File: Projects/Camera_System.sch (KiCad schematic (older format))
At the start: 10 parts, among them J1 BARREL_JACK, U1 IFX1117ME_V33, U2 LD2980ABM50TR

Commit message: Component and footprint library created
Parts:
- U1: footprint (none) -> MyLibraries:IFX1117ME_V33
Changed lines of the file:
@@
 LIBS:atmel
 LIBS:contrib
+LIBS:valves
 LIBS:MyLibrary
-LIBS:valves
 LIBS:Camera_System-cache
 EELAYER 25 0
@@
 Text Notes 3250 1200 0    60   ~ 0
 6 < VIN < 15
-$Comp
-L IFX1117ME_V33 U1
-U 1 1 59131708
-P 4450 1150
-F 0 "U1" H 4450 1250 60  0000 C CNN
-F 1 "IFX1117ME_V33" H 4450 1400 60  0000 C CNN
-F 2 "" H 4450 1150 60  0001 C CNN
-F 3 "" H 4450 1150 60  0001 C CNN
-	1    4450 1150
-	1    0    0    -1
-$EndComp
 Wire Wire Line
 	5000 1300 5900 1300
@@
 Wire Wire Line
 	5900 2850 5900 2750
-$Comp
-L LD2980ABM50TR U2
-U 1 1 59132F80
-P 4450 2750
-F 0 "U2" H 4450 2900 60  0000 C CNN
-F 1 "LD2980ABM50TR" H 4450 3050 60  0000 C CNN
-F 2 "" H 4450 2750 60  0001 C CNN
-F 3 "" H 4450 2750 60  0001 C CNN
-	1    4450 2750
-	1    0    0    -1
-$EndComp
 Text Notes 4100 2350 0    60   ~ 0
 Order the one with fixed output voltage = 5V
@@
 Text Label 2600 1300 0    60   ~ 0
 VDC_IN
+$Comp
+L IFX1117ME_V33 U1
+U 1 1 59135F80
+P 4450 1150
+F 0 "U1" H 4450 1250 60  0000 C CNN
+F 1 "IFX1117ME_V33" H 4450 1400 60  0000 C CNN
+F 2 "MyLibraries:IFX1117ME_V33" H 4450 1150 60  0001 C CNN
+F 3 "" H 4450 1150 60  0001 C CNN
+	1    4450 1150
+	1    0    0    -1
+$EndComp
+$Comp
+L LD2980ABM50TR U2
+U 1 1 59135FEA
+P 4450 2750
+F 0 "U2" H 4450 2900 60  0000 C CNN
+F 1 "LD2980ABM50TR" H 4450 3050 60  0000 C CNN
+F 2 "" H 4450 2750 60  0001 C CNN
+F 3 "" H 4450 2750 60  0001 C CNN
+	1    4450 2750
+	1    0    0    -1
+$EndComp
 $EndSCHEMATC

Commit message: Power Management Layout Created
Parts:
- removed D1: CS3D, symbol D
- added D1: CS3M, MyLibraries:CS3M, symbol CS3M
- C1: footprint (none) -> MyLibraries:UWT1E470MCL6GS
- C2: footprint (none) -> MyLibraries:UWX1E100MCL1GB
- C3, C4, C6: footprint (none) -> Capacitors_SMD:C_0603_HandSoldering
- C5: footprint (none) -> Capacitors_SMD:C_0805_HandSoldering
- J1: footprint (none) -> MyLibraries:PJ-002B
- U2: footprint (none) -> MyLibraries:LD2980ABM50TR
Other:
- note added: "I_out = 1.1A"
- note added: "I_out = 50mA"
- note removed: "I_out_min = 1.1A"
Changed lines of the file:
@@
 F 0 "J1" H 1050 1595 50  0000 C CNN
 F 1 "BARREL_JACK" H 1050 1245 50  0000 C CNN
-F 2 "" H 1050 1400 50  0001 C CNN
+F 2 "MyLibraries:PJ-002B" H 1050 1400 50  0001 C CNN
 F 3 "" H 1050 1400 50  0001 C CNN
 	1    1050 1400
@@
 Wire Wire Line
 	1350 1300 1900 1300
-$Comp
-L CP C1
-U 1 1 5912CF48
-P 2400 1650
-F 0 "C1" H 2425 1750 50  0000 L CNN
-F 1 "47u" H 2425 1550 50  0000 L CNN
-F 2 "" H 2438 1500 50  0001 C CNN
-F 3 "" H 2400 1650 50  0001 C CNN
-	1    2400 1650
-	1    0    0    -1
-$EndComp
 Wire Wire Line
 	2400 1300 2400 1500
@@
 Wire Wire Line
 	2400 1800 2400 1900
-$Comp
-L D D1
-U 1 1 5912D262
-P 2050 1300
-F 0 "D1" H 2050 1400 50  0000 C CNN
-F 1 "CS3D" H 2050 1200 50  0000 C CNN
-F 2 "" H 2050 1300 50  0001 C CNN
-F 3 "" H 2050 1300 50  0001 C CNN
-	1    2050 1300
-	-1   0    0    1
-$EndComp
 Connection ~ 2400 1300
 Wire Wire Line
 	2200 1300 3900 1300
-Wire Wire Line
-	5550 1500 5550 1300
 Wire Wire Line
 	5550 1800 5550 1900
@@
 F 0 "C4" H 3625 1750 50  0000 L CNN
 F 1 "100n" H 3625 1550 50  0000 L CNN
-F 2 "" H 3638 1500 50  0001 C CNN
+F 2 "Capacitors_SMD:C_0603_HandSoldering" H 3638 1500 50  0001 C CNN
 F 3 "" H 3600 1650 50  0001 C CNN
 	1    3600 1650
@@
 Order the one with fixed output voltage = 3.3V
 Text Notes 5000 1200 0    60   ~ 0
-I_out_min = 1.1A
+I_out = 1.1A
 $Comp
 L CP C2
@@
 F 0 "C2" H 3275 1750 50  0000 L CNN
 F 1 "10u" H 3275 1550 50  0000 L CNN
-F 2 "" H 3288 1500 50  0001 C CNN
+F 2 "MyLibraries:UWX1E100MCL1GB" H 3288 1500 50  0001 C CNN
 F 3 "" H 3250 1650 50  0001 C CNN
 	1    3250 1650
@@
 F 0 "C6" H 5575 3300 50  0000 L CNN
 F 1 "2.2u" H 5575 3100 50  0000 L CNN
-F 2 "" H 5588 3050 50  0001 C CNN
+F 2 "Capacitors_SMD:C_0603_HandSoldering" H 5588 3050 50  0001 C CNN
 F 3 "" H 5550 3200 50  0001 C CNN
 	1    5550 3200
@@
 F 0 "C3" H 3275 3300 50  0000 L CNN
 F 1 "1u" H 3275 3100 50  0000 L CNN
-F 2 "" H 3288 3050 50  0001 C CNN
+F 2 "Capacitors_SMD:C_0603_HandSoldering" H 3288 3050 50  0001 C CNN
 F 3 "" H 3250 3200 50  0001 C CNN
 	1    3250 3200
@@
 F 0 "C5" H 5575 1750 50  0000 L CNN
 F 1 "22u" H 5575 1550 50  0000 L CNN
-F 2 "" H 5588 1500 50  0001 C CNN
+F 2 "Capacitors_SMD:C_0805_HandSoldering" H 5588 1500 50  0001 C CNN
 F 3 "" H 5550 1650 50  0001 C CNN
 	1    5550 1650
@@
 F 0 "U2" H 4450 2900 60  0000 C CNN
 F 1 "LD2980ABM50TR" H 4450 3050 60  0000 C CNN
-F 2 "" H 4450 2750 60  0001 C CNN
+F 2 "MyLibraries:LD2980ABM50TR" H 4450 2750 60  0001 C CNN
 F 3 "" H 4450 2750 60  0001 C CNN
 	1    4450 2750
 	1    0    0    -1
 $EndComp
+Text Notes 4950 2700 0    60   ~ 0
+I_out = 50mA
+$Comp
+L CS3M D1
+U 1 1 591418FD
+P 2050 1300
+F 0 "D1" H 2050 1400 50  0000 C CNN
+F 1 "CS3M" H 2050 1200 50  0000 C CNN
+F 2 "MyLibraries:CS3M" H 2050 1300 50  0001 C CNN
+F 3 "" H 2050 1300 50  0001 C CNN
+	1    2050 1300
+	-1   0    0    1
+$EndComp
+$Comp
+L CP C1
+U 1 1 591435A8
+P 2400 1650
+F 0 "C1" H 2425 1750 50  0000 L CNN
+F 1 "47u" H 2425 1550 50  0000 L CNN
+F 2 "MyLibraries:UWT1E470MCL6GS" H 2438 1500 50  0001 C CNN
+F 3 "" H 2400 1650 50  0001 C CNN
+	1    2400 1650
+	1    0    0    -1
+$EndComp
+Wire Wire Line
+	5550 1300 5550 1500
+Connection ~ 5550 1300
 $EndSCHEMATC

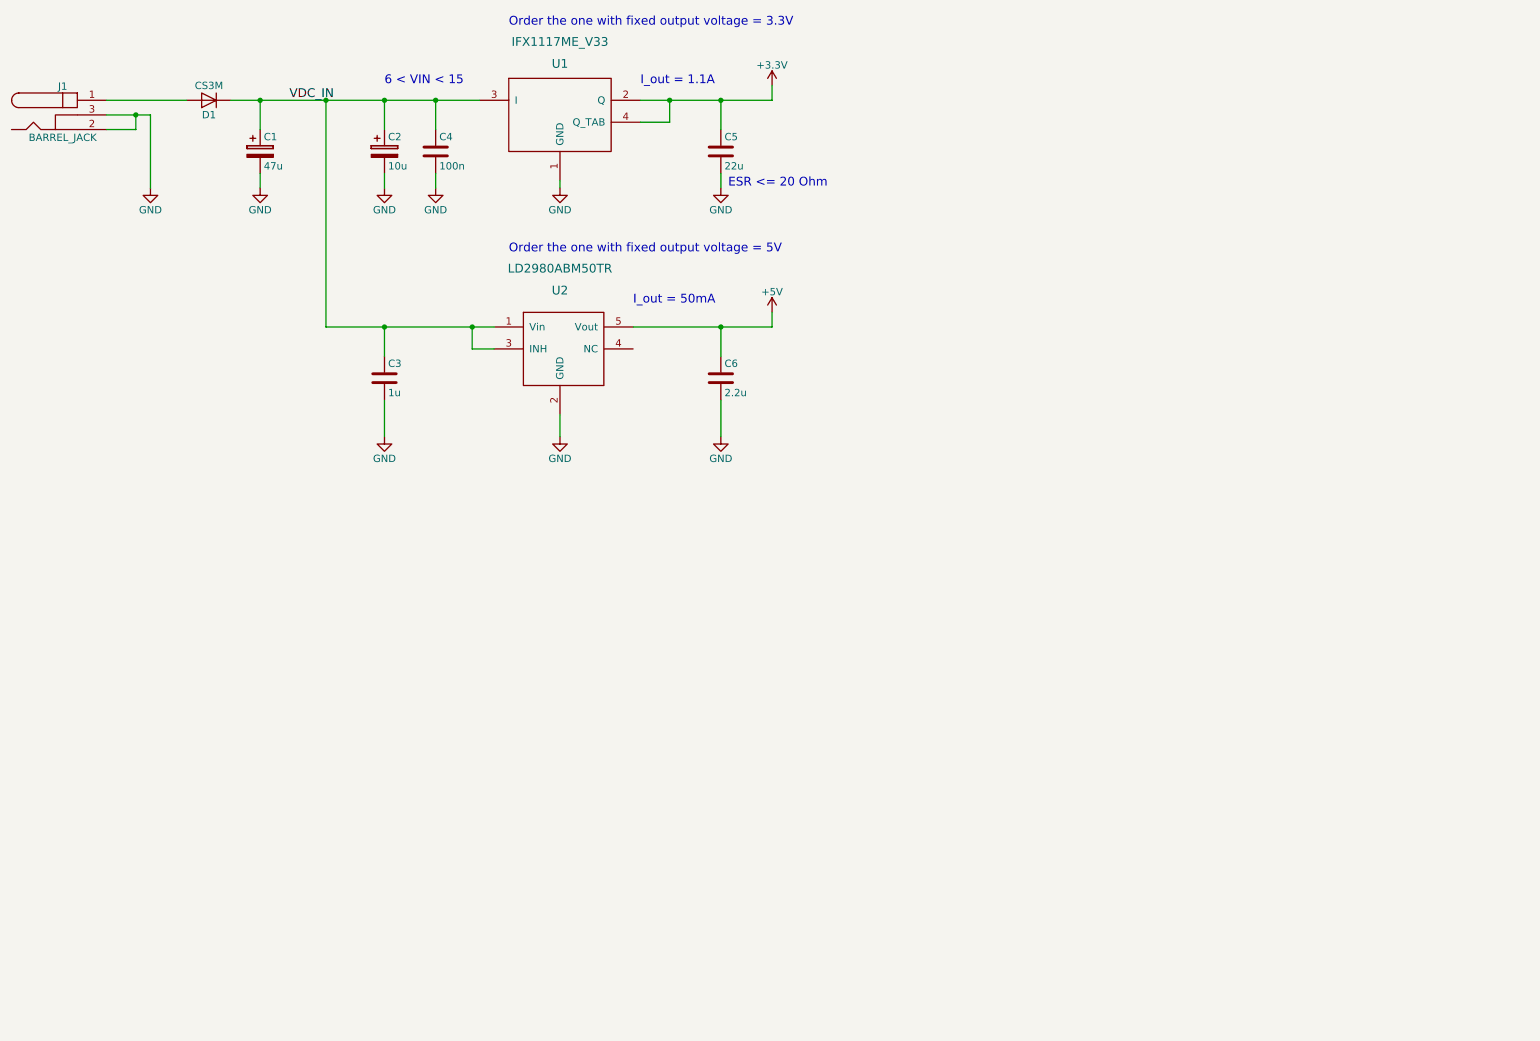
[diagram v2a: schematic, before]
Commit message: New symbols habe been added
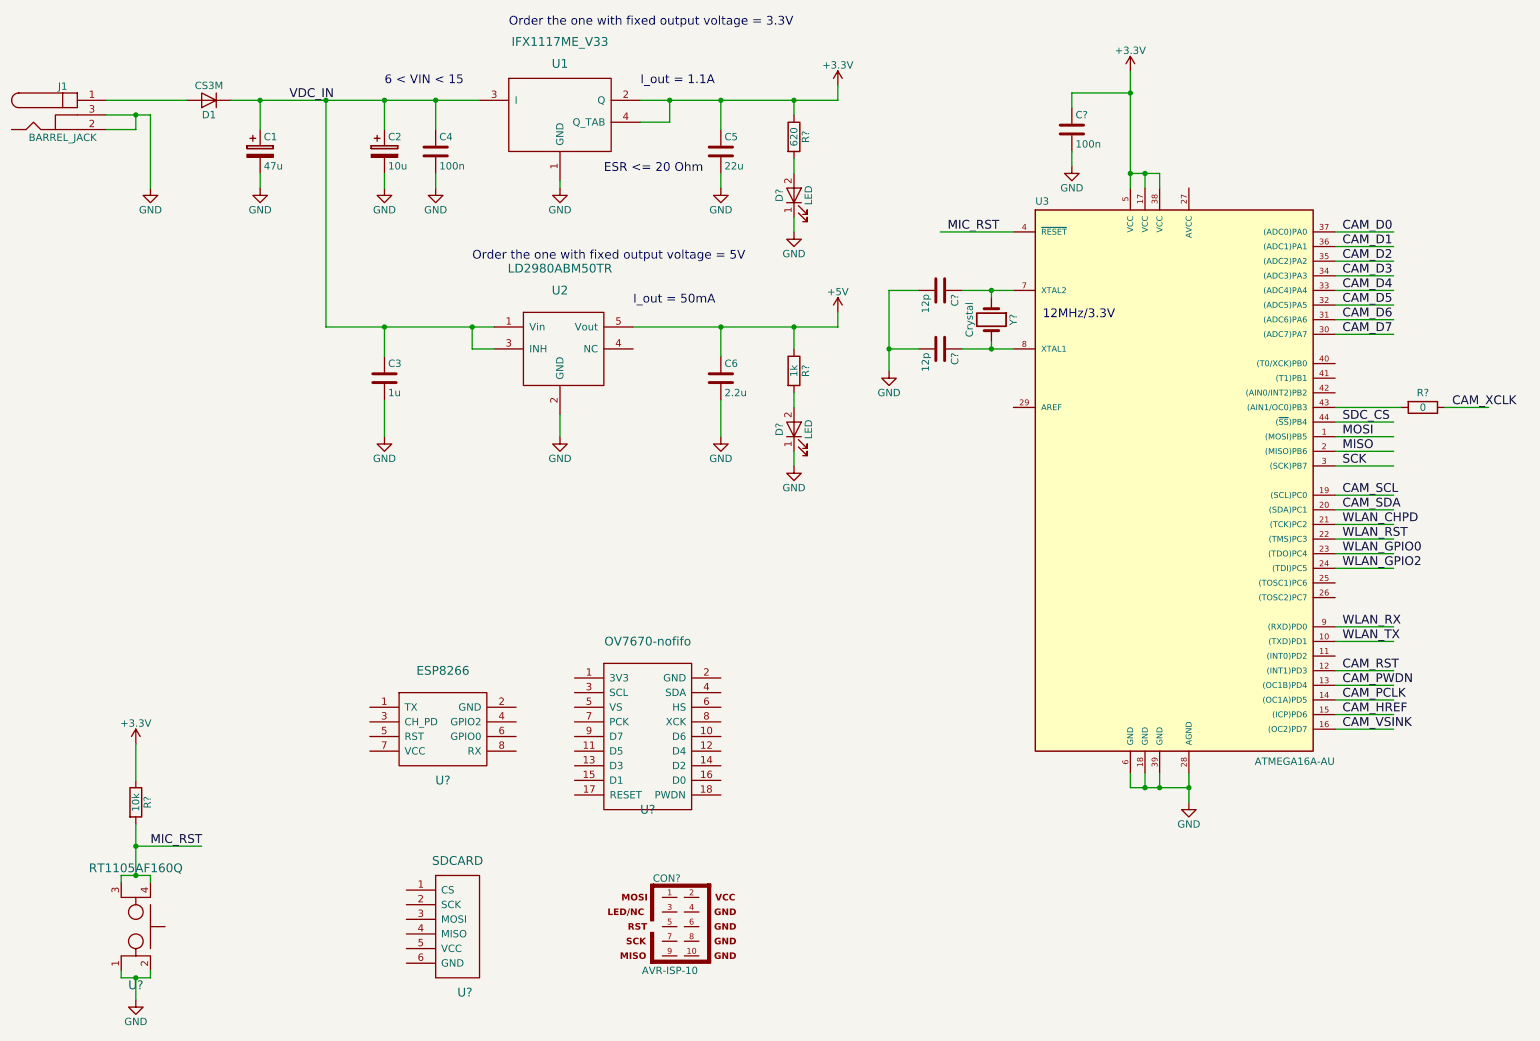
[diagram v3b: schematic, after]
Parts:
- added C?: 100n, Capacitors_SMD:C_0805_HandSoldering, symbol C
- added C? (x2): 12p, Capacitors_SMD:C_0603_HandSoldering, symbol C
- added CON?: AVR-ISP-10, AVR-ISP-10, symbol AVR-ISP-10
- added D? (x2): LED, symbol LED
- added R?: 620, symbol R
- added R?: 1k, symbol R
- added R?: 0, symbol R
- added R?: 10k, symbol R
- added U3: ATMEGA16A-AU, MyLibraries:ATMEGA16A-AU, symbol ATMEGA16A-AU
- added U?: RT1105AF160Q, symbol RT1105AF160Q
- added U?: ESP8266, symbol ESP8266
- added U?: OV7670-nofifo, symbol OV7670-nofifo
- added U?: SDCARD, symbol SDCARD
- added Y?: Crystal, symbol Crystal
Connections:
- net labels added: CAM_D0, CAM_D1, CAM_D2, CAM_D3, CAM_D4, CAM_D5, CAM_D6, CAM_D7, CAM_HREF, CAM_PCLK, CAM_PWDN, CAM_RST, CAM_SCL, CAM_SDA, CAM_VSINK, CAM_XCLK, MIC_RST, MISO, MOSI, SCK, SDC_CS, WLAN_CHPD, WLAN_GPIO0, WLAN_GPIO2, WLAN_RST, WLAN_RX, WLAN_TX
- wire segments 30 -> 93
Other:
- note added: "12MHz/3.3V\n"

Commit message: Schematic for additional modules have been created
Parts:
- removed U3: ATMEGA16A-AU, MyLibraries:ATMEGA16A-AU, symbol ATMEGA16A-AU
- added C? (x9): 100n, Capacitors_SMD:C_0805_HandSoldering, symbol C
- added D?: LED, symbol LED
- added R?: 620, symbol R
- added R? (x2): 4.7k, symbol R
- added R?: 24.9, symbol R
- added R? (x7): 10k, symbol R
- added R? (x2): 1.74k, symbol R
- added R?: 200k, symbol R
- added U?: ATMEGA16A-AU, TQFP44, symbol ATMEGA16A-AU
- added U?: Si501, symbol Si501
- added U?: CD4014B, symbol CD4014B
- added U? (x6): RT1105AF160Q, symbol RT1105AF160Q
- added U?: LCD_1602, symbol LCD_1602
- added U?: PCA9306, symbol PCA9306
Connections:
- net labels added: 3V3_SCL, 3V3_SDA, 5V_SCL, 5V_SDA, CAM_VSINC, CTRL_BTN1, CTRL_BTN2, CTRL_DOWN, CTRL_LEFT, CTRL_RIGHT, CTRL_UP, P_S_CLK, P_S_CTRL, SERIAL_IN
- net labels removed: CAM_SCL, CAM_SDA, CAM_VSINK
- wire segments 93 -> 271
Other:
- note added: "BUTTONS"
- note added: "CAMERA"
- note added: "LCD"
- note added: "Modules"
- note added: "SD CARD"
- note added: "WLAN"
- moved on the sheet: C?, CON?, R?, U?, Y?

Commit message: New footprints have been created
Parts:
- CON1: renamed from CON?; footprint AVR-ISP-10 -> MyLibraries:N2510-6002RB
- D2, D3, D4: renamed from D?; footprint (none) -> LEDs:LED_0603
- R1, R10, R11, R12, R13, R14, R15, R16, R17, R18, R2, R3, R4, R5, R6, R7, R8, R9: renamed from R?; footprint (none) -> Resistors_SMD:R_0603_HandSoldering
- U10, U11, U13, U4, U5, U6, U7: renamed from U?; footprint (none) -> MyLibraries:RT1105AF160Q
- U8: renamed from U?; footprint (none) -> MyLibraries:CD4014B_SOIC
- U9: renamed from U?; footprint (none) -> MyLibraries:PCA9306_SM8
- gave numbers to parts that had none: 19

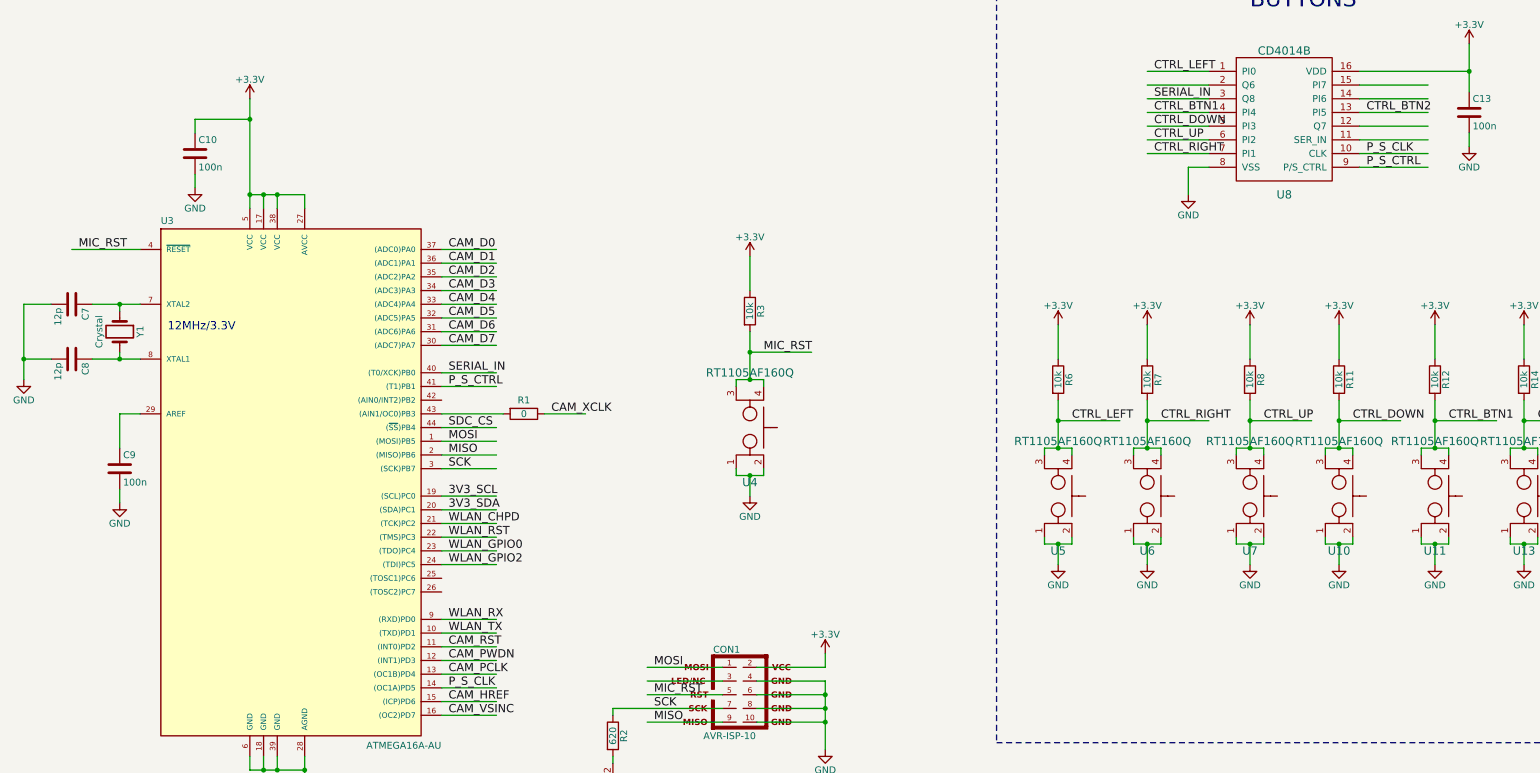
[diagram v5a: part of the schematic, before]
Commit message: Schematic has been finished and layout started
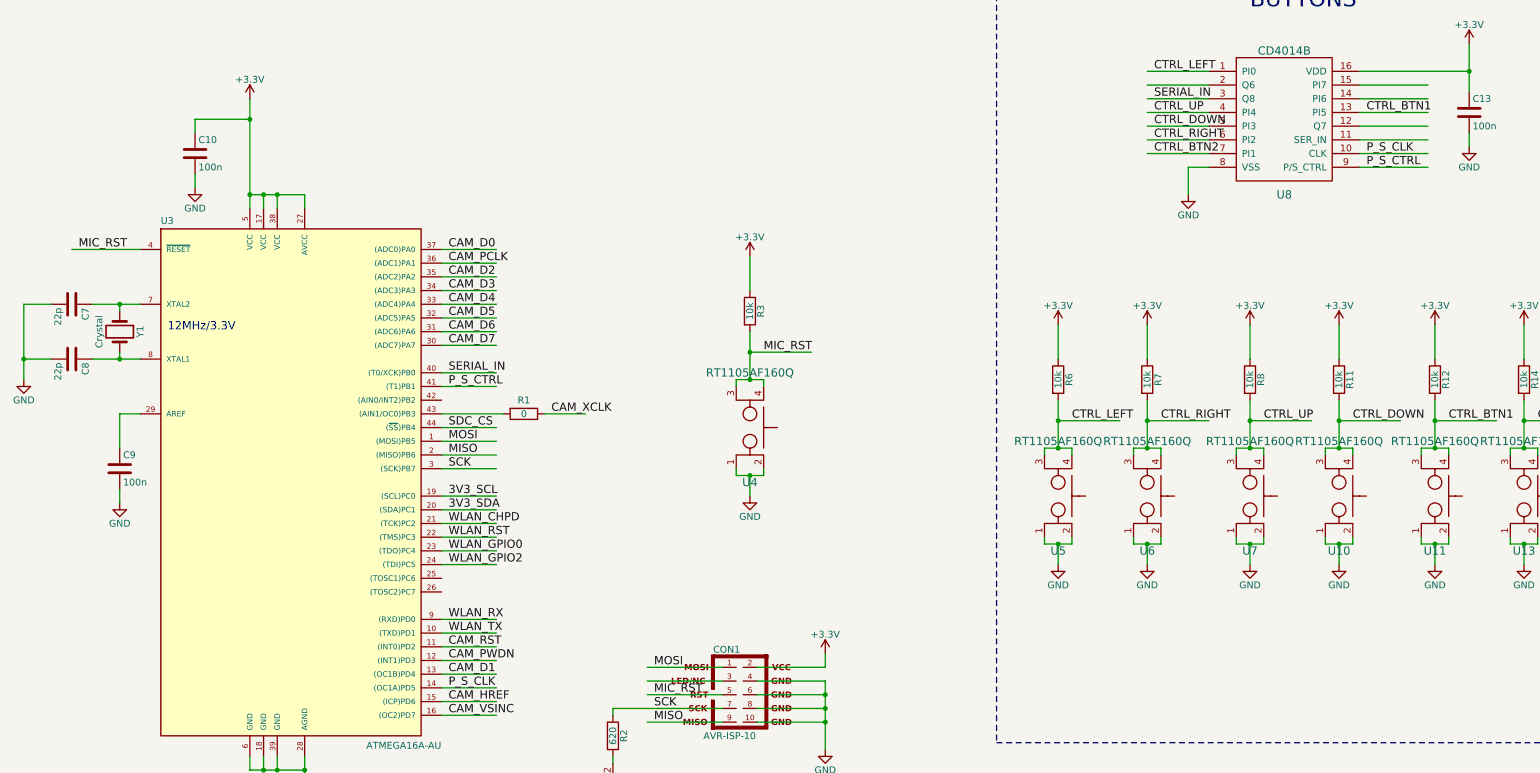
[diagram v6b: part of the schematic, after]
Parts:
- C7, C8: value 12p -> 22p
- U12: footprint (none) -> MyLibraries:LCD_header_2.5_4
- U14: footprint (none) -> MyLibraries:Si501_2x2.5
- U15: footprint (none) -> MyLibraries:Camera_ov7670_2.5_2x9
- U16: footprint (none) -> MyLibraries:wifi_header_female_2.5_2x4
- U17: footprint (none) -> MyLibraries:SDCARD_2.5_6
- U3: footprint TQFP44 -> MyLibraries:ATMEGA16A-AU
- Y1: footprint (none) -> MyLibraries:LFXTAL003210
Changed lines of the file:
@@
 Text Label 3800 6350 0    60   ~ 0
 CAM_D0
-Text Label 3800 6450 0    60   ~ 0
+Text Label 3800 9450 0    60   ~ 0
 CAM_D1
 Text Label 3800 6550 0    60   ~ 0
@@
 F 0 "Y1" H 1400 7100 50  0000 C CNN
 F 1 "Crystal" H 1400 6800 50  0000 C CNN
-F 2 "" H 1400 6950 50  0001 C CNN
+F 2 "MyLibraries:LFXTAL003210" H 1400 6950 50  0001 C CNN
 F 3 "" H 1400 6950 50  0001 C CNN
 	1    1400 6950
@@
 P 1050 6750
 F 0 "C7" H 1075 6850 50  0000 L CNN
-F 1 "12p" H 1075 6650 50  0000 L CNN
+F 1 "22p" H 1075 6650 50  0000 L CNN
 F 2 "Capacitors_SMD:C_0603_HandSoldering" H 1088 6600 50  0001 C CNN
 F 3 "" H 1050 6750 50  0001 C CNN
@@
 P 1050 7150
 F 0 "C8" H 1075 7250 50  0000 L CNN
-F 1 "12p" H 1075 7050 50  0000 L CNN
+F 1 "22p" H 1075 7050 50  0000 L CNN
 F 2 "Capacitors_SMD:C_0603_HandSoldering" H 1088 7000 50  0001 C CNN
 F 3 "" H 1050 7150 50  0001 C CNN
@@
 Text Label 3800 9350 0    60   ~ 0
 CAM_PWDN
-Text Label 3800 9450 0    60   ~ 0
+Text Label 3800 6450 0    60   ~ 0
 CAM_PCLK
 Text Label 3800 9650 0    60   ~ 0
@@
 F 0 "U16" H 14300 5300 60  0000 C CNN
 F 1 "ESP8266" H 14300 6050 60  0000 C CNN
-F 2 "" H 14300 5900 60  0001 C CNN
+F 2 "MyLibraries:wifi_header_female_2.5_2x4" H 14300 5900 60  0001 C CNN
 F 3 "" H 14300 5900 60  0001 C CNN
 	1    14300 5900
@@
 F 0 "U15" H 14200 1000 60  0000 C CNN
 F 1 "OV7670-nofifo" H 14200 2250 60  0000 C CNN
-F 2 "" H 14200 2100 60  0001 C CNN
+F 2 "MyLibraries:Camera_ov7670_2.5_2x9" H 14200 2100 60  0001 C CNN
 F 3 "" H 14200 2100 60  0001 C CNN
 	1    14200 2100
@@
 F 0 "U17" H 14600 7400 60  0000 C CNN
 F 1 "SDCARD" H 14550 8300 60  0000 C CNN
-F 2 "" H 14700 8200 60  0001 C CNN
+F 2 "MyLibraries:SDCARD_2.5_6" H 14700 8200 60  0001 C CNN
 F 3 "" H 14700 8200 60  0001 C CNN
 	1    14700 8200
@@
 F 0 "U3" H 1700 9930 50  0000 L BNN
 F 1 "ATMEGA16A-AU" H 3200 6100 50  0000 L BNN
-F 2 "TQFP44" H 2650 8050 50  0001 C CIN
+F 2 "MyLibraries:ATMEGA16A-AU" H 2650 8050 50  0001 C CIN
 F 3 "" H 2650 8050 50  0001 C CNN
 	1    2650 8050
@@
 F 0 "U14" H 14050 3350 60  0000 C CNN
 F 1 "Si501" H 14050 3850 60  0000 C CNN
-F 2 "" H 14050 3750 60  0001 C CNN
+F 2 "MyLibraries:Si501_2x2.5" H 14050 3750 60  0001 C CNN
 F 3 "" H 14050 3750 60  0001 C CNN
 	1    14050 3750
@@
 Text Label 8950 5050 0    60   ~ 0
 CTRL_LEFT
-Text Label 8950 5650 0    60   ~ 0
+Text Label 8950 5550 0    60   ~ 0
 CTRL_RIGHT
-Text Label 8950 5550 0    60   ~ 0
+Text Label 8950 5350 0    60   ~ 0
 CTRL_UP
 Text Label 8950 5450 0    60   ~ 0
 CTRL_DOWN
-Text Label 8950 5350 0    60   ~ 0
+Text Label 10500 5350 0    60   ~ 0
 CTRL_BTN1
-Text Label 10500 5350 0    60   ~ 0
+Text Label 8950 5650 0    60   ~ 0
 CTRL_BTN2
 Text Label 3800 9550 0    60   ~ 0
@@
 F 0 "U12" H 11050 1100 60  0000 C CNN
 F 1 "LCD_1602" H 11050 1800 60  0000 C CNN
-F 2 "" H 11200 1700 60  0001 C CNN
+F 2 "MyLibraries:LCD_header_2.5_4" H 11200 1700 60  0001 C CNN
 F 3 "" H 11200 1700 60  0001 C CNN
 	1    11200 1700
